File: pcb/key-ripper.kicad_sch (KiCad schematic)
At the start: 205 parts, among them J1 Conn_01x03, SW1 ESC, SW10 F9, SW11 F10, SW12 F11, SW13 F12, SW14 TILDE, SW15 1, SW16 2, SW17 3, SW18 4, SW19 5, SW2 F1, SW20 6, SW21 7, SW22 8, SW23 9, SW24 0, SW25 -, SW26 =, SW27 BACKSPACE, SW28 TAB, SW29 Q, SW3 F2, SW30 W, SW31 E, SW32 R, SW33 T, SW34 Y, SW35 U, SW36 I, SW37 O, SW38 P, SW39 [, SW4 F3, SW40 ], SW41 \, SW42 CAPS, SW43 A, SW44 S, SW45 D, SW46 F, SW47 G, SW48 H, SW49 J, SW5 F4, SW50 K, SW51 L, SW52 ;, SW53 ', SW54 ENTER, SW55 L_SHIFT, SW56 Z, SW57 X, SW58 C, SW59 V, SW6 F5, SW60 B, SW61 N, SW62 M, SW63 ,, SW64 ., SW65 /, SW66 UP, SW67 FN, SW68 BL_CTRL, SW69 L_ALT, SW7 F6, SW70 L_CMD, SW71 SPACE, SW72 R_CMD, SW73 LEFT, SW74 DOWN, SW75 RIGHT, SW8 F7, SW9 F8, U1 RP2040, U2 TYPE-C-31-M-12, U3 XC6206PxxxMR, U4 W25Q128JVS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

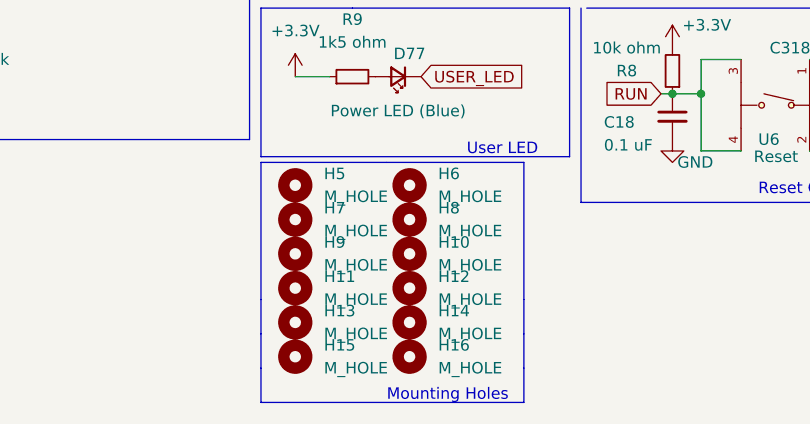
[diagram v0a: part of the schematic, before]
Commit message: Remove M2 mounting holes
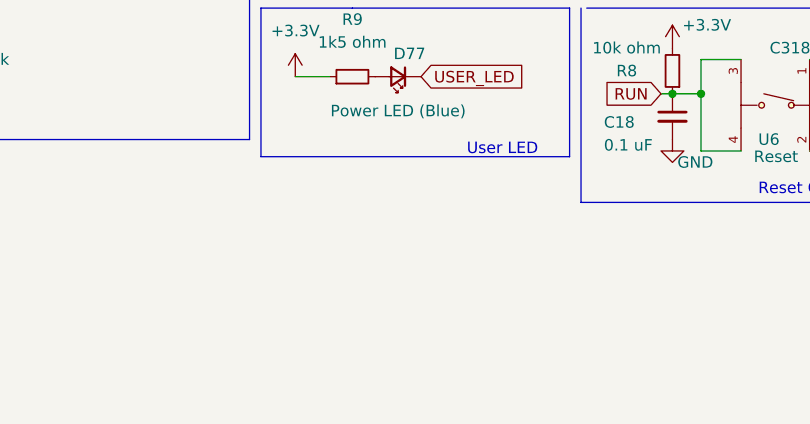
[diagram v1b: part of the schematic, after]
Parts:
- removed H10, H11, H12, H13, H14, H15, H16, H5, H6, H7, H8, H9: M_HOLE, MountingHole:MountingHole_2.2mm_M2, symbol Mechanical:MountingHole
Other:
- note removed: "Mounting Holes"

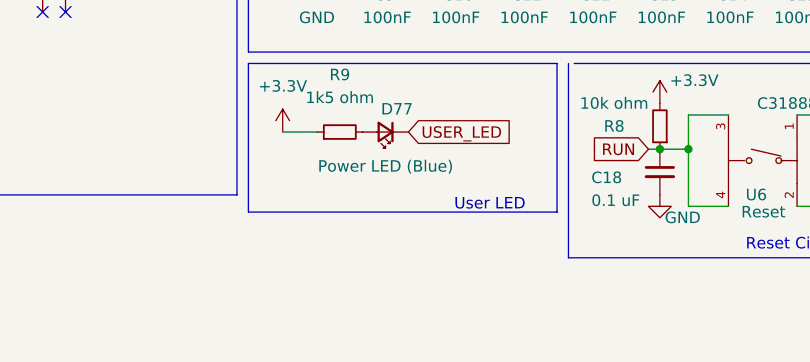
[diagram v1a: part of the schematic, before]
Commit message: Add threaded PCB insertsj, clean up switch matrix wiring
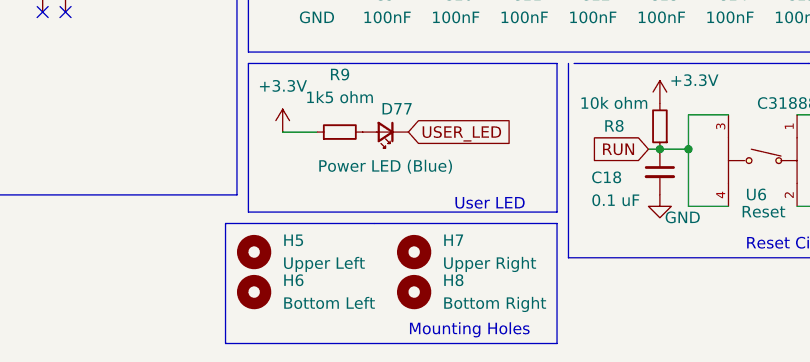
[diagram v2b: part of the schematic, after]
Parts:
- added H5: Upper Left, footprints:threaded_insert_m3_24939, symbol Mechanical:MountingHole
- added H6: Bottom Left, footprints:threaded_insert_m3_24939, symbol Mechanical:MountingHole
- added H7: Upper Right, footprints:threaded_insert_m3_24939, symbol Mechanical:MountingHole
- added H8: Bottom Right, footprints:threaded_insert_m3_24939, symbol Mechanical:MountingHole
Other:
- note added: "Mounting Holes"
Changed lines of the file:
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@@
     (stroke (width 0) (type default) (color 0 0 0 0))
   )
+  (polyline (pts (xy 88.9 195.58) (xy 52.07 195.58))
+    (stroke (width 0) (type default) (color 0 0 0 0))
+  )
   (wire (pts (xy -1.905 53.34) (xy 0.635 53.34))
     (stroke (width 0) (type default) (color 0 0 0 0))
@@
     (stroke (width 0) (type default) (color 0 0 0 0))
   )
+  (polyline (pts (xy 88.9 182.245) (xy 88.9 195.58))
+    (stroke (width 0) (type default) (color 0 0 0 0))
+  )
   (polyline (pts (xy 190.5 111.76) (xy 190.5 140.335))
     (stroke (width 0) (type default) (color 0 0 0 0))
@@
     (stroke (width 0) (type default) (color 0 0 0 0))
   )
+  (polyline (pts (xy 68.58 182.245) (xy 88.9 182.245))
+    (stroke (width 0) (type default) (color 0 0 0 0))
+  )
   (wire (pts (xy 234.95 36.83) (xy 234.95 49.53))
     (stroke (width 0) (type default) (color 0 0 0 0))
@@
     (stroke (width 0) (type default) (color 0 0 0 0))
   )
+  (polyline (pts (xy 52.07 195.58) (xy 52.07 182.245))
+    (stroke (width 0) (type default) (color 0 0 0 0))
+  )
   (polyline (pts (xy 128.27 140.335) (xy 128.27 111.76))
     (stroke (width 0) (type default) (color 0 0 0 0))
@@
     (stroke (width 0) (type default) (color 0 0 0 0))
   )
+  (polyline (pts (xy 52.07 182.245) (xy 68.58 182.245))
+    (stroke (width 0) (type default) (color 0 0 0 0))
+  )
   (wire (pts (xy 92.71 154.305) (xy 100.33 154.305))
     (stroke (width 0) (type default) (color 0 0 0 0))
@@
     (effects (font (size 1.27 1.27)) (justify left bottom))
   )
+  (text "Mounting Holes" (at 72.39 194.945 0)
+    (effects (font (size 1.27 1.27)) (justify left bottom))
+  )
   (text "1uF caps near VREG_IN and VREG_OUT" (at -109.22 22.225 0)
     (effects (font (size 1.27 1.27)) (justify left bottom))
@@
     (pin "2")
   )
+  (symbol (lib_id "Mechanical:MountingHole") (at 55.245 189.865 0) (unit 1)
+    (in_bom yes) (on_board yes) (fields_autoplaced)
+    (property "Reference" "H6" (id 0) (at 58.42 188.5949 0)
+      (effects (font (size 1.27 1.27)) (justify left))
+    )
+    (property "Value" "Bottom Left" (id 1) (at 58.42 191.1349 0)
+      (effects (font (size 1.27 1.27)) (justify left))
+    )
+    (property "Footprint" "footprints:threaded_insert_m3_24939" (id 2) (at 55.245 189.865 0)
+      (effects (font (size 1.27 1.27)) hide)
+    )
+    (property "Datasheet" "~" (id 3) (at 55.245 189.865 0)
+      (effects (font (size 1.27 1.27)) hide)
+    )
+  )
   (symbol (lib_id "Device:D_Small") (at 209.55 39.37 90) (unit 1)
     (in_bom yes) (on_board yes)
@@
     (pin "1")
   )
+  (symbol (lib_id "Mechanical:MountingHole") (at 73.025 185.42 0) (unit 1)
+    (in_bom yes) (on_board yes) (fields_autoplaced)
+    (property "Reference" "H7" (id 0) (at 76.2 184.1499 0)
+      (effects (font (size 1.27 1.27)) (justify left))
+    )
+    (property "Value" "Upper Right" (id 1) (at 76.2 186.6899 0)
+      (effects (font (size 1.27 1.27)) (justify left))
+    )
+    (property "Footprint" "footprints:threaded_insert_m3_24939" (id 2) (at 73.025 185.42 0)
+      (effects (font (size 1.27 1.27)) hide)
+    )
+    (property "Datasheet" "~" (id 3) (at 73.025 185.42 0)
+      (effects (font (size 1.27 1.27)) hide)
+    )
+  )
   (symbol (lib_id "Device:D_Small") (at 133.35 77.47 90) (unit 1)
     (in_bom yes) (on_board yes)
@@
     (pin "2")
   )
+  (symbol (lib_id "Mechanical:MountingHole") (at 73.025 189.865 0) (unit 1)
+    (in_bom yes) (on_board yes) (fields_autoplaced)
+    (property "Reference" "H8" (id 0) (at 76.2 188.5949 0)
+      (effects (font (size 1.27 1.27)) (justify left))
+    )
+    (property "Value" "Bottom Right" (id 1) (at 76.2 191.1349 0)
+      (effects (font (size 1.27 1.27)) (justify left))
+    )
+    (property "Footprint" "footprints:threaded_insert_m3_24939" (id 2) (at 73.025 189.865 0)
+      (effects (font (size 1.27 1.27)) hide)
+    )
+    (property "Datasheet" "~" (id 3) (at 73.025 189.865 0)
+      (effects (font (size 1.27 1.27)) hide)
+    )
+  )
   (symbol (lib_id "Switch:SW_Push") (at 46.99 36.83 0) (unit 1)
     (in_bom yes) (on_board yes) (fields_autoplaced)
@@
     (pin "2")
   )
+  (symbol (lib_id "Mechanical:MountingHole") (at 55.245 185.42 0) (unit 1)
+    (in_bom yes) (on_board yes) (fields_autoplaced)
+    (property "Reference" "H5" (id 0) (at 58.42 184.1499 0)
+      (effects (font (size 1.27 1.27)) (justify left))
+    )
+    (property "Value" "Upper Left" (id 1) (at 58.42 186.6899 0)
+      (effects (font (size 1.27 1.27)) (justify left))
+    )
+    (property "Footprint" "footprints:threaded_insert_m3_24939" (id 2) (at 55.245 185.42 0)
+      (effects (font (size 1.27 1.27)) hide)
+    )
+    (property "Datasheet" "~" (id 3) (at 55.245 185.42 0)
+      (effects (font (size 1.27 1.27)) hide)
+    )
+  )
   (symbol (lib_id "Device:D_Schottky_Small") (at 68.58 123.19 180) (unit 1)
     (in_bom yes) (on_board yes)
@@
       (reference "H4") (unit 1) (value "BACKSPACE_STABILIZER") (footprint "bschwind_stabilizers:cherry_mx_stabilizer_2.00u")
     )
+    (path "/ee7809c2-9dfe-481d-a797-6cb8a9f0fa3d"
+      (reference "H5") (unit 1) (value "Upper Left") (footprint "footprints:threaded_insert_m3_24939")
+    )
+    (path "/182b3ef0-34d9-4d5d-994f-22fbf8f997e0"
+      (reference "H6") (unit 1) (value "Bottom Left") (footprint "footprints:threaded_insert_m3_24939")
+    )
+    (path "/9323b259-375c-47b8-a40c-b5acb14cd1f1"
+      (reference "H7") (unit 1) (value "Upper Right") (footprint "footprints:threaded_insert_m3_24939")
+    )
+    (path "/b349b2db-497d-4c6b-8940-c2edf6033d3a"
+      (reference "H8") (unit 1) (value "Bottom Right") (footprint "footprints:threaded_insert_m3_24939")
+    )
     (path "/1b5afd94-2096-4603-93d6-8693d1fb5da2"

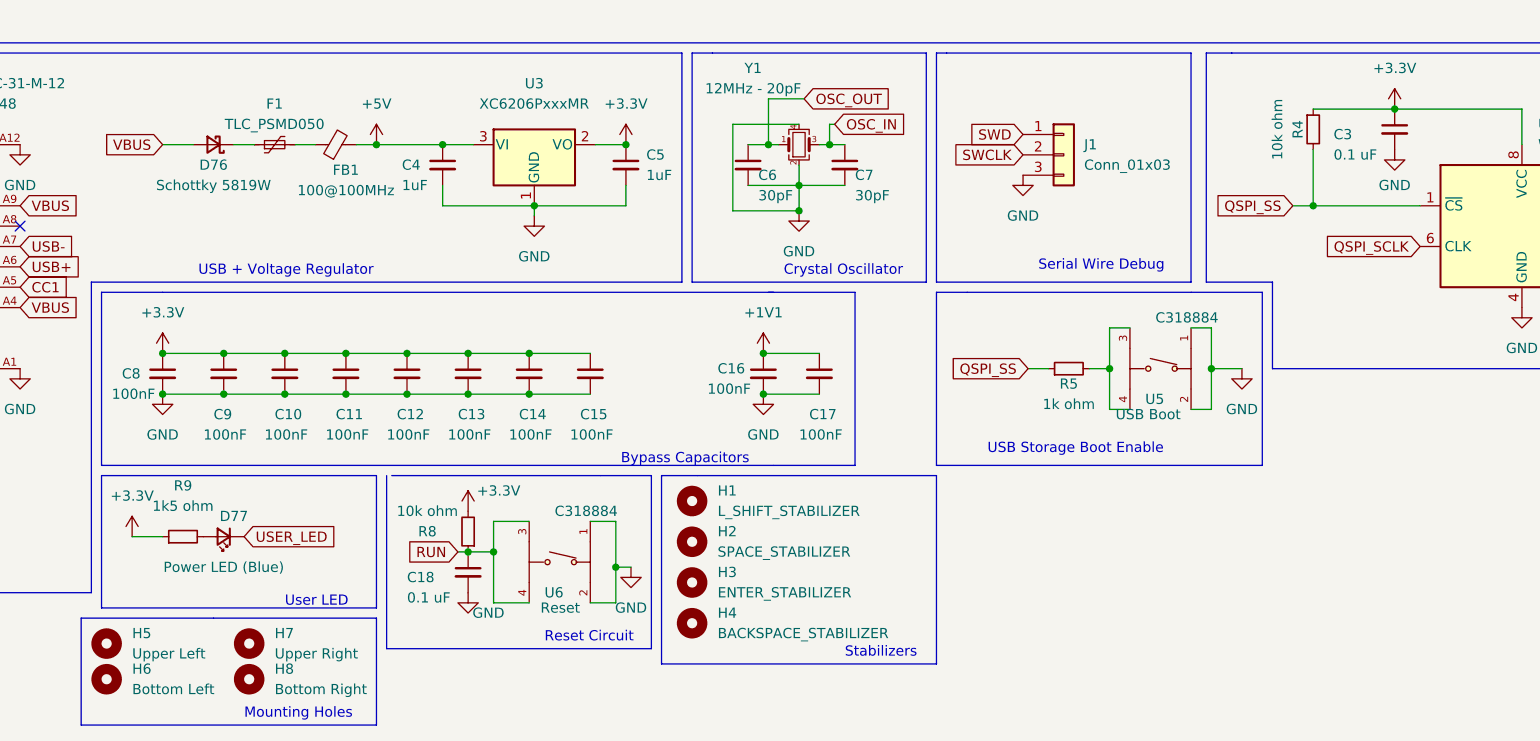
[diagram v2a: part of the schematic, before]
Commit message: Slightly consolidate passive values
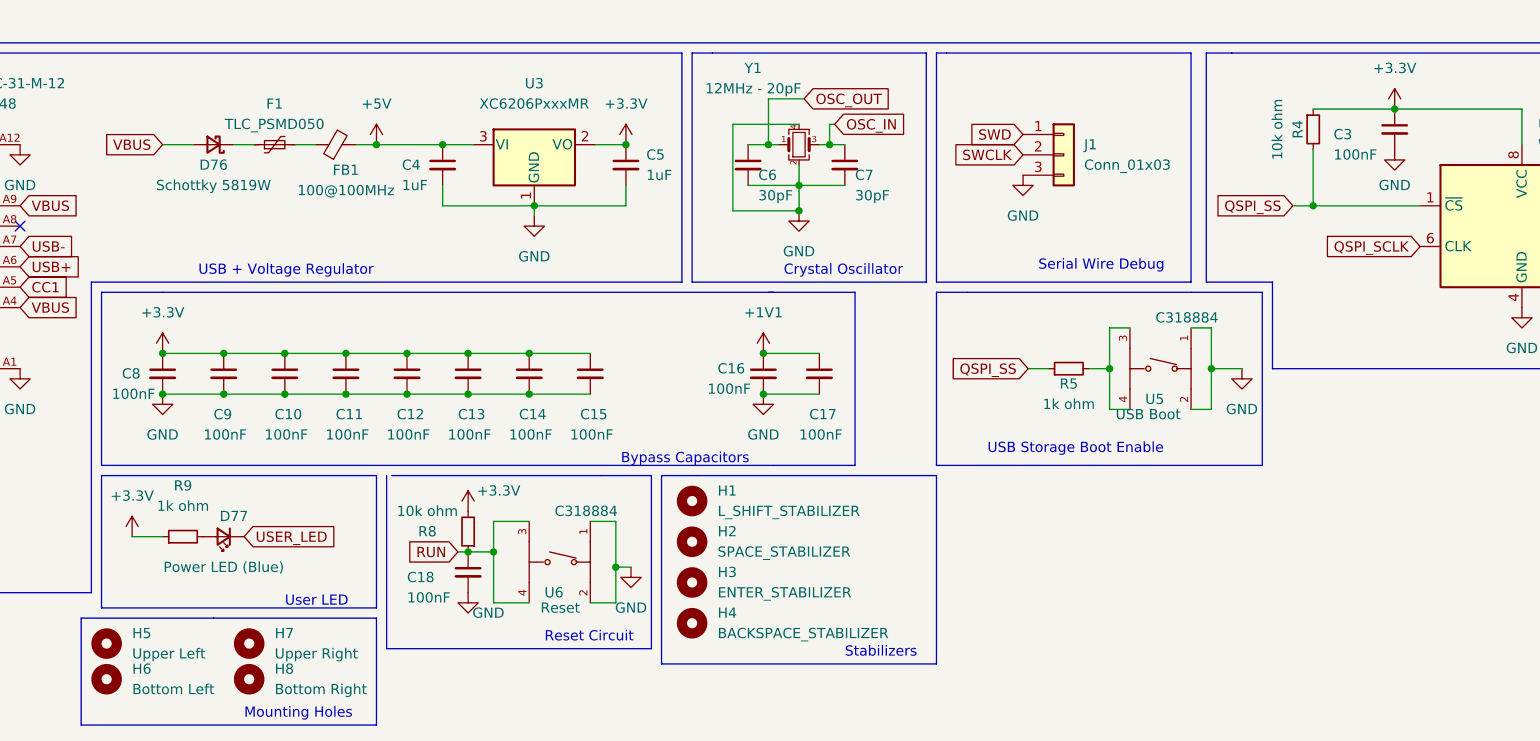
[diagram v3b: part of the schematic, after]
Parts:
- C18, C3: value 0.1 uF -> 100nF
- R9: value 1k5 ohm -> 1k ohm
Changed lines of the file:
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@@
       (effects (font (size 1.27 1.27)) (justify left))
     )
-    (property "Value" "0.1 uF" (id 1) (at 92.71 179.705 0)
+    (property "Value" "100nF" (id 1) (at 92.71 179.705 0)
       (effects (font (size 1.27 1.27)) (justify left))
     )
@@
     (in_bom yes) (on_board yes) (fields_autoplaced)
     (property "Reference" "R9" (id 0) (at 64.77 165.735 90))
-    (property "Value" "1k5 ohm" (id 1) (at 64.77 168.275 90))
+    (property "Value" "1k ohm" (id 1) (at 64.77 168.275 90))
     (property "Footprint" "Resistor_SMD:R_0402_1005Metric" (id 2) (at 64.77 172.085 0)
       (effects (font (size 1.27 1.27)) hide)
@@
       (effects (font (size 1.27 1.27)) (justify left))
     )
-    (property "Value" "0.1 uF" (id 1) (at 208.28 124.46 0)
+    (property "Value" "100nF" (id 1) (at 208.28 124.46 0)
       (effects (font (size 1.27 1.27)) (justify left))
     )
@@
     )
     (path "/e2a270d9-b44d-424f-bb20-8c5ce86072d8"
-      (reference "C3") (unit 1) (value "0.1 uF") (footprint "Capacitor_SMD:C_0402_1005Metric")
+      (reference "C3") (unit 1) (value "100nF") (footprint "Capacitor_SMD:C_0402_1005Metric")
     )
     (path "/96cb0cd6-ffa9-444f-8cc1-1b5160745ac6"
@@
     )
     (path "/423b905c-bafe-4d42-b1dc-969145b11c60"
-      (reference "C18") (unit 1) (value "0.1 uF") (footprint "Capacitor_SMD:C_0402_1005Metric")
+      (reference "C18") (unit 1) (value "100nF") (footprint "Capacitor_SMD:C_0402_1005Metric")
     )
     (path "/af119a18-3250-43e9-881b-9a53617d7d1d"
@@
     )
     (path "/556ef9ca-0364-4889-be76-ec9d7d5619ff"
-      (reference "R9") (unit 1) (value "1k5 ohm") (footprint "Resistor_SMD:R_0402_1005Metric")
+      (reference "R9") (unit 1) (value "1k ohm") (footprint "Resistor_SMD:R_0402_1005Metric")
     )
     (path "/e7893166-2c2c-41b4-bd84-76ebc2e06551"
